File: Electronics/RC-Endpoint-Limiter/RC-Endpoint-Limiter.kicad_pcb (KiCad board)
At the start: 2 copper layers, 46.8 x 29.9 mm, 44 parts, among them J1 USB_B_Micro, J2 Aux Low, J3 Aux High, J4 Switch Low, J5 Switch High, J6 RC Input, J7 RC Output, J8 Inhibit Input, U1 ATmega32U4-MU, Y1 8Mhz

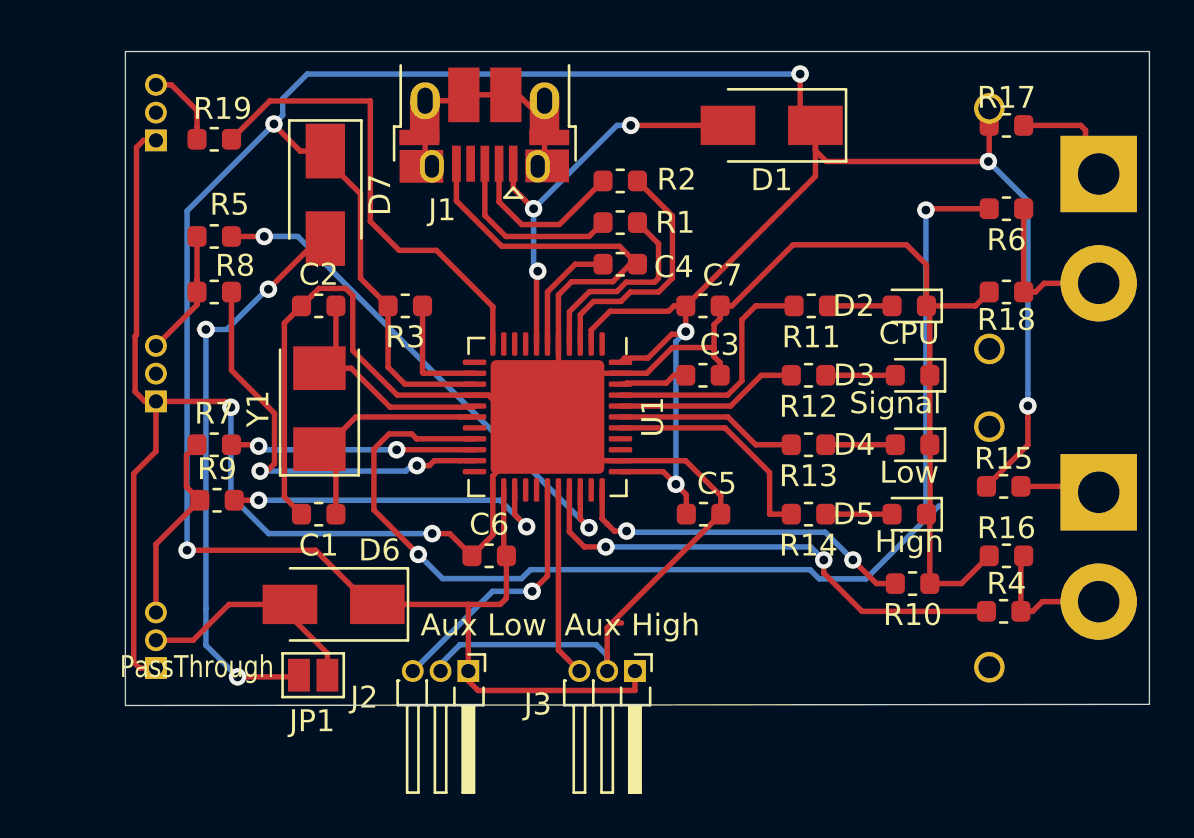
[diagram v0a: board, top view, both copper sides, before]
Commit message: made aux inputs dedicated hall inputs, Make sure to enable pullups,  bit low on board space around there to fit external pullup resistors added fuses.
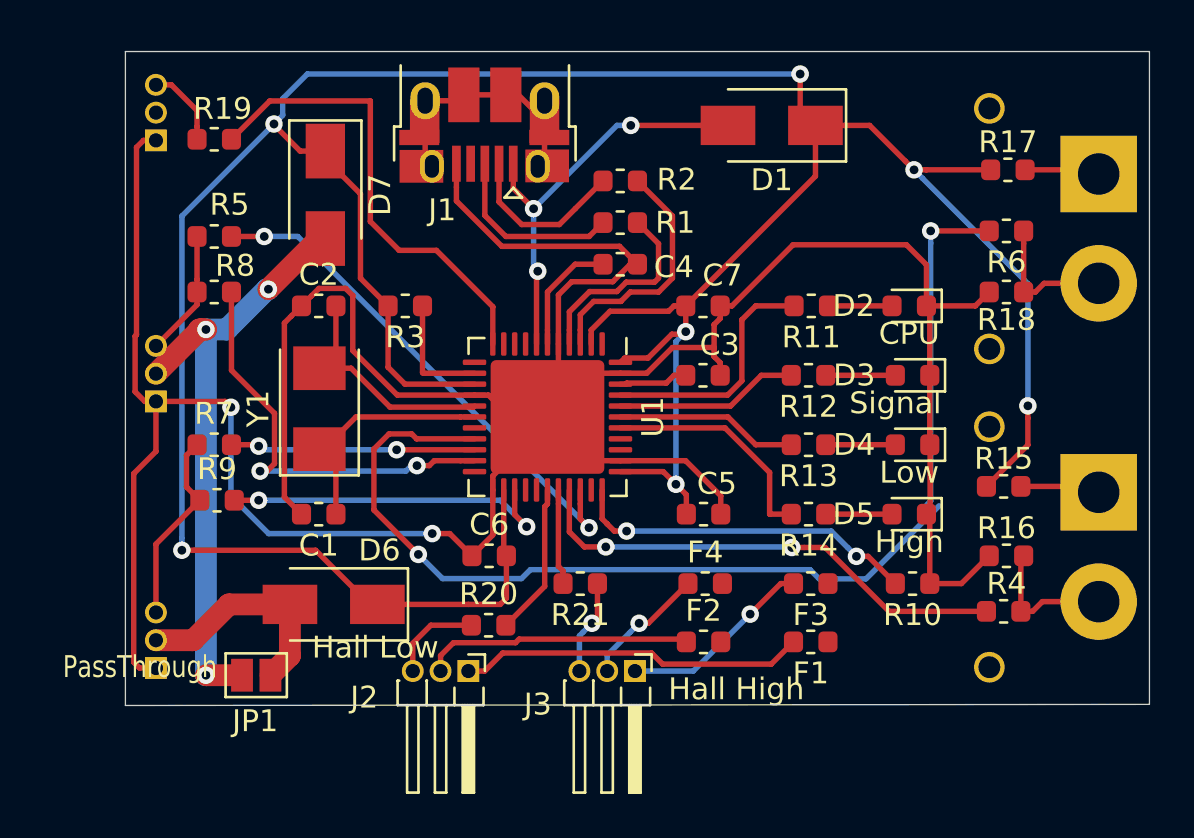
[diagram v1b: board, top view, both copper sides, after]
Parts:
- added F1: 0.5A, Fuse:Fuse_0603_1608Metric, F.Cu at (116.2, 63.6)
- added F2: 0.5A, Fuse:Fuse_0603_1608Metric, F.Cu at (111.3, 63.6)
- added F3: 0.5A, Fuse:Fuse_0603_1608Metric, F.Cu at (116.2, 61.0)
- added F4: 0.5A, Fuse:Fuse_0603_1608Metric, F.Cu at (111.4, 61.0)
- added R20: 1K, Resistor_SMD:R_0603_1608Metric, F.Cu at (101.4, 62.9)
- added R21: 1K, Resistor_SMD:R_0603_1608Metric, F.Cu at (105.6, 61.0)
- J2: value Aux Low -> Hall Low
- J3: value Aux High -> Hall High
- moved JP1 2.60 mm to (90.8, 65.2)
- moved R17 2.03 mm to (125.2, 42.0)
- moved R6 1.02 mm to (125.1, 44.8)
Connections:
- J2 pad 1: VCC -> Net-(F1-Pad2)
- J2 pad 2: GND -> Net-(F2-Pad1)
- J3 pad 1: VCC -> Net-(F3-Pad2)
- J3 pad 2: GND -> Net-(F4-Pad1)
- U1 pad 28: Net-(J2-Pad3) -> Net-(R20-Pad2)
- U1 pad 29: Net-(J3-Pad3) -> Net-(R21-Pad2)
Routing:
- net GND: track 174.9 -> 155.9 mm
- net Net-(F1-Pad2): track 0.00 -> 15.8 mm
- net VCC: track 160.2 -> 147.3 mm
- net Net-(F2-Pad1): track 0.00 -> 12.6 mm
- net Net-(F3-Pad2): track 0.00 -> 8.91 mm, vias 0 -> 1
- net Net-(J2-Pad3): track 12.1 -> 4.51 mm, vias 1 -> 0
- net Net-(R20-Pad2): track 0.00 -> 6.98 mm
- net Net-(F4-Pad1): track 0.00 -> 5.78 mm, vias 0 -> 1
- net Net-(R21-Pad2): track 0.00 -> 4.37 mm
- net Net-(J3-Pad3): track 8.68 -> 4.34 mm, vias 0 -> 1
- net Net-(J5-Pad1): track 4.92 -> 3.44 mm
- net Net-(D7-Pad2): track 26.8 -> 28.1 mm
- net Net-(R6-Pad2): track 53.1 -> 52.0 mm
- net Net-(J5-Pad2): track 6.81 -> 5.79 mm

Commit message: added lots more I/O
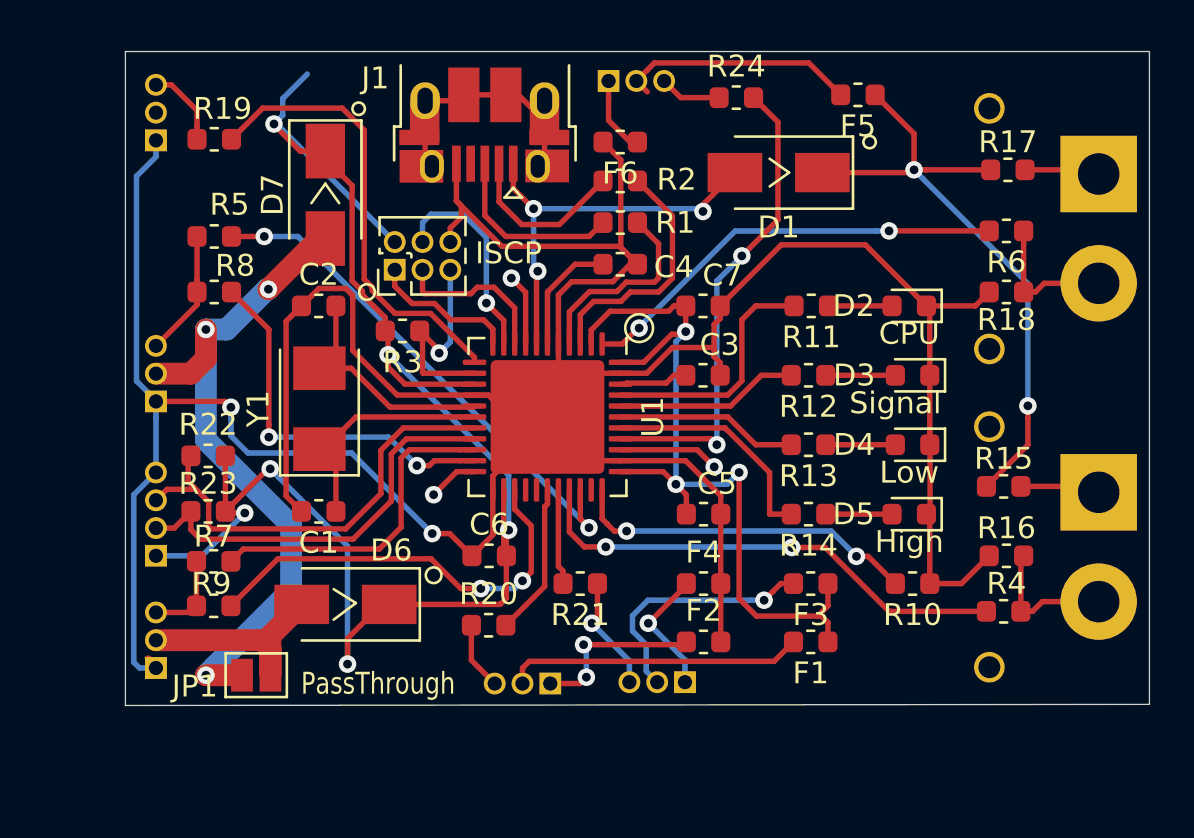
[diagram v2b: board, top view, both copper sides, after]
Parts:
- added F5: 0.5A, Fuse:Fuse_0603_1608Metric, F.Cu at (118.3, 38.6)
- added F6: 0.5A, Fuse:Fuse_0603_1608Metric, F.Cu at (107.5, 40.8)
- added J10: ISCP, Connector_PinHeader_1.27mm:PinHeader_2x03_P1.27mm_Vertical, F.Cu at (97.2, 46.6)
- added J11: POT Input, Connector_PinHeader_1.27mm:PinHeader_1x03_P1.27mm_Horizontal, B.Cu at (106.9, 38.0)
- added J9: I²C header, Connector_PinHeader_1.27mm:PinHeader_1x04_P1.27mm_Horizontal, B.Cu at (86.2, 59.7)
- added R22: 10K, Resistor_SMD:R_0603_1608Metric, F.Cu at (88.6, 55.1)
- added R23: 10K, Resistor_SMD:R_0603_1608Metric, F.Cu at (88.6, 57.7)
- added R24: 1K, Resistor_SMD:R_0603_1608Metric, F.Cu at (112.8, 38.7)
- J2, J3: moved to B.Cu
- moved R7 5.33 mm to (88.9, 59.9)
- moved R9 4.83 mm to (88.9, 62.0)
- moved J2 3.79 mm to (104.3, 65.5), turned to 90 degrees
- moved J3 2.34 mm to (110.4, 65.5), turned to 90 degrees
- moved D1 2.18 mm to (114.7, 42.2)
- moved R3 1.15 mm to (97.5, 49.4)
- moved D6 0.54 mm to (94.9, 61.9)
- moved C1 0.13 mm to (93.7, 57.7)
- moved F4 0.08 mm to (111.3, 61.0)
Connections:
- net Net-(R3-Pad1) renamed /RESET
- J2 pad 1: Net-(F1-Pad2) -> Net-(F2-Pad1)
- J2 pad 2: Net-(F2-Pad1) -> Net-(F1-Pad2)
- J3 pad 1: Net-(F3-Pad2) -> Net-(F4-Pad1)
- J3 pad 2: Net-(F4-Pad1) -> Net-(F3-Pad2)
- U1 pad 1: Net-(U1-Pad1) -> Net-(R6-Pad2)
- U1 pad 10: Net-(U1-Pad10) -> /MOSI
- U1 pad 11: Net-(R19-Pad2) -> /MISO
- U1 pad 12: Net-(U1-Pad12) -> Net-(R19-Pad2)
- U1 pad 19: Net-(R6-Pad2) -> Net-(J9-Pad2)
- U1 pad 9: Net-(U1-Pad9) -> /SCK
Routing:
- net Net-(R6-Pad2): track 52.0 -> 19.8 mm
- net Net-(R24-Pad2): track 0.00 -> 22.0 mm, vias 0 -> 2
- net Net-(J9-Pad3): track 0.00 -> 20.9 mm
- net Net-(J9-Pad2): track 0.00 -> 19.1 mm
- net Net-(F5-Pad2): track 0.00 -> 11.0 mm
- net GND: track 155.9 -> 166.9 mm
- net /MOSI: track 0.00 -> 9.61 mm, vias 0 -> 1
- net /SCK: track 0.00 -> 7.43 mm
- net /MISO: track 0.00 -> 6.73 mm
- net Net-(J6-Pad3): track 8.95 -> 4.01 mm
- net Net-(U1-Pad36): track 0.00 -> 4.61 mm, vias 0 -> 1
- net Net-(F2-Pad1): track 12.6 -> 8.24 mm, vias 0 -> 2
- net Net-(R7-Pad2): track 11.2 -> 15.1 mm, vias 2 -> 0
- net /RESET: track 5.44 -> 9.33 mm, vias 0 -> 1
- net Net-(R9-Pad2): track 15.8 -> 19.6 mm
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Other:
- board text added: "+"
- board text added: "-"
- board text added: "C"
- board text added: "D"
- board text added: "S"

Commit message: polished up PCB layout
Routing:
- net GND: track 166.9 -> 204.6 mm, vias 2 -> 12
- net VCC: track 144.2 -> 176.8 mm, vias 11 -> 13
- net /RESET: track 9.33 -> 7.00 mm
- net Net-(D1-Pad2): track 18.9 -> 20.1 mm
- net Net-(D7-Pad2): track 31.8 -> 30.8 mm
- net Net-(R6-Pad2): track 19.8 -> 20.8 mm
- net Net-(J1-Pad3): track 8.43 -> 7.53 mm
- net Net-(J9-Pad3): track 20.9 -> 21.7 mm
- net Net-(R10-Pad2): track 16.0 -> 15.2 mm
- net Net-(J9-Pad2): track 19.1 -> 19.8 mm
- net Net-(R24-Pad2): track 22.0 -> 22.6 mm
- net Net-(J1-Pad2): track 7.76 -> 7.24 mm
- added copper zone on B.Cu, net GND
- added copper zone on F.Cu, net VCC
